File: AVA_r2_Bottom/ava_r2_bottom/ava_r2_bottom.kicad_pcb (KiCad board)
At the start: 2 copper layers, 52 x 72 mm, 29 parts, among them J1 RC_Radio, J2 UART_RxTx_5V, J3 I2C_SdaScl_3V, J4 5V_IN, J5 GND_IN, J6 SER1_SER2, J7 SER3_SER4, J8 SER5_SER6, U1 MPU6500, U2 Teensy4.1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

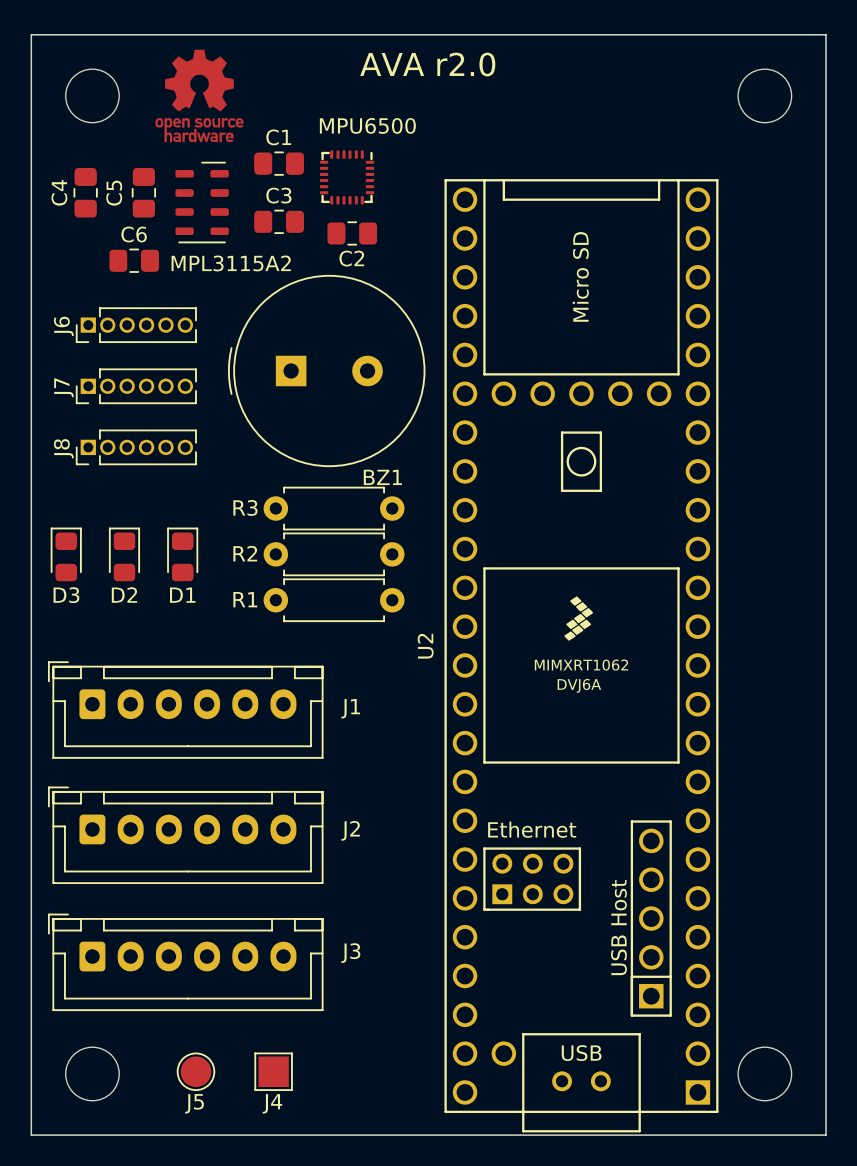
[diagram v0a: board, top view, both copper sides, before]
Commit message: PCB Bottom Complete
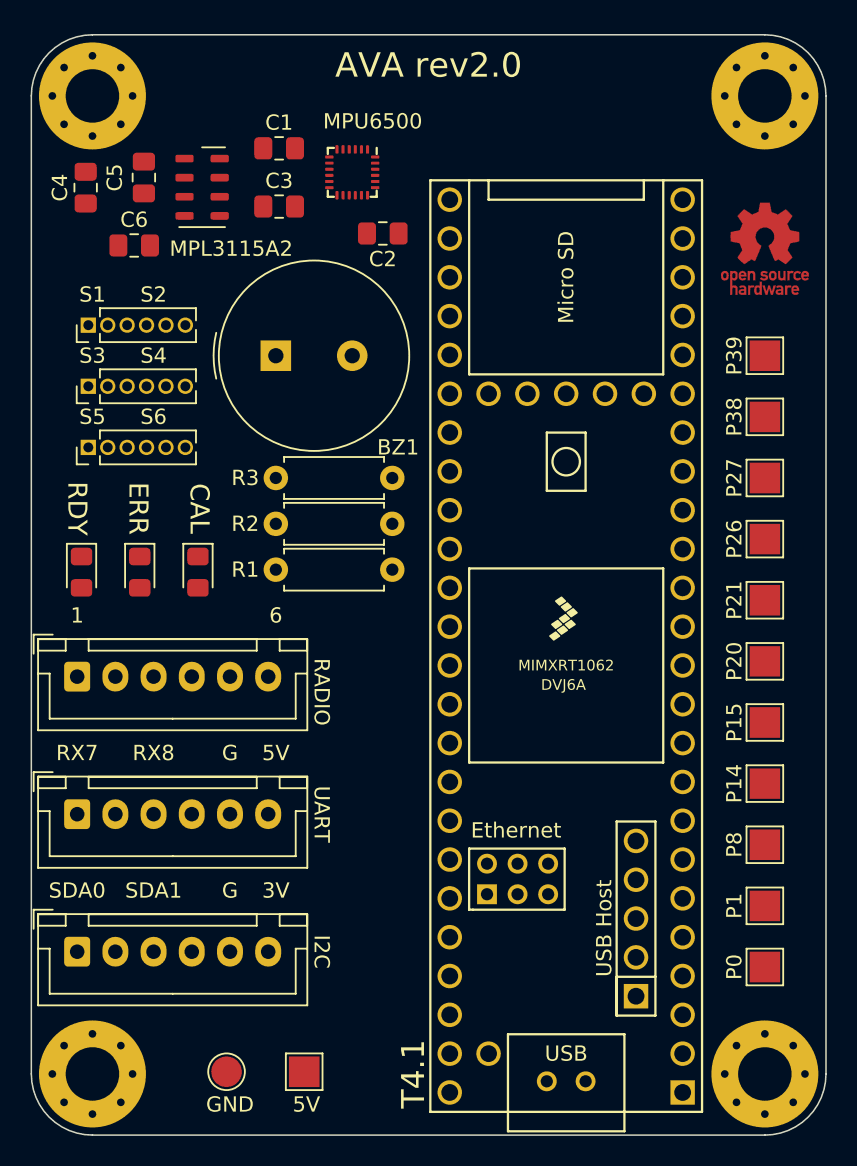
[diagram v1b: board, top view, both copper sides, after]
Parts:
- removed J1: RC_Radio, Connector_JST:JST_XH_B6B-XH-A_1x06_P2.50mm_Vertical
- removed J2: UART_RxTx_5V, Connector_JST:JST_XH_B6B-XH-A_1x06_P2.50mm_Vertical
- removed J3: I2C_SdaScl_3V, Connector_JST:JST_XH_B6B-XH-A_1x06_P2.50mm_Vertical
- removed the REF** at (184.0, 112.0)
- removed the REF** at (228.0, 112.0)
- removed the REF** at (228.0, 48.0)
- removed the REF** at (184.0, 48.0)
- added I2C1: I2C_SdaScl_3V, Connector_JST:JST_XH_B6B-XH-A_1x06_P2.50mm_Vertical, F.Cu at (183.0, 104.0)
- added P0: TestPoint, TestPoint:TestPoint_Pad_2.0x2.0mm, F.Cu at (228.0, 105.0)
- added P1: TestPoint, TestPoint:TestPoint_Pad_2.0x2.0mm, F.Cu at (228.0, 101.0)
- added P14: TestPoint, TestPoint:TestPoint_Pad_2.0x2.0mm, F.Cu at (228.0, 93.0)
- added P15: TestPoint, TestPoint:TestPoint_Pad_2.0x2.0mm, F.Cu at (228.0, 89.0)
- added P20: TestPoint, TestPoint:TestPoint_Pad_2.0x2.0mm, F.Cu at (228.0, 85.0)
- added P21: TestPoint, TestPoint:TestPoint_Pad_2.0x2.0mm, F.Cu at (228.0, 81.0)
- added P26: TestPoint, TestPoint:TestPoint_Pad_2.0x2.0mm, F.Cu at (228.0, 77.0)
- added P27: TestPoint, TestPoint:TestPoint_Pad_2.0x2.0mm, F.Cu at (228.0, 73.0)
- added P38: TestPoint, TestPoint:TestPoint_Pad_2.0x2.0mm, F.Cu at (228.0, 69.0)
- added P39: TestPoint, TestPoint:TestPoint_Pad_2.0x2.0mm, F.Cu at (228.0, 65.0)
- added P8: TestPoint, TestPoint:TestPoint_Pad_2.0x2.0mm, F.Cu at (228.0, 97.0)
- added RADIO1: RC_Radio, Connector_JST:JST_XH_B6B-XH-A_1x06_P2.50mm_Vertical, F.Cu at (183.0, 86.0)
- added REF**: MountingHole_3.5mm_Pad_Via, MountingHole:MountingHole_3.5mm_Pad_Via, F.Cu at (228.0, 112.0)
- added REF**: MountingHole_3.5mm_Pad_Via, MountingHole:MountingHole_3.5mm_Pad_Via, F.Cu at (184.0, 112.0)
- added REF**: MountingHole_3.5mm_Pad_Via, MountingHole:MountingHole_3.5mm_Pad_Via, F.Cu at (184.0, 48.0)
- added REF**: MountingHole_3.5mm_Pad_Via, MountingHole:MountingHole_3.5mm_Pad_Via, F.Cu at (228.0, 48.0)
- added UART1: UART_RxTx_5V, Connector_JST:JST_XH_B6B-XH-A_1x06_P2.50mm_Vertical, F.Cu at (183.0, 95.0)
- moved REF** 38.3 mm to (228.0, 58.0)
- moved C2 2.00 mm to (203.0, 57.0)
- moved J4 2.00 mm to (197.9, 111.9)
- moved J5 2.00 mm to (192.8, 111.9)
- moved R1 2.00 mm to (196.0, 79.0)
- moved R2 2.00 mm to (196.0, 76.0)
- moved R3 2.00 mm to (196.0, 73.0)
- moved BZ1 1.41 mm to (196.0, 65.0)
- moved D1 1.41 mm to (190.9, 79.2)
- moved D2 1.41 mm to (187.1, 79.2)
- moved D3 1.41 mm to (183.3, 79.2)
- moved C1 1.00 mm to (196.2, 51.4)
- moved C3 1.00 mm to (196.2, 55.2)
- moved C5 1.00 mm to (187.4, 53.3)
- moved C6 1.00 mm to (186.7, 57.8)
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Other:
- outline, holes or cut-outs redrawn
- board text added: "1"
- board text added: "3V"
- board text added: "5V"
- board text added: "6"
- board text added: "AVA rev2.0"
- board text added: "CAL"
- board text added: "ERR"
- board text added: "G"
- board text added: "GND"
- board text added: "I2C"
- board text added: "RADIO"
- board text added: "RDY"
- board text added: "RX7"
- board text added: "RX8"
- board text added: "S1"
- board text added: "S2"
- board text added: "S3"
- board text added: "S4"
- board text added: "S5"
- board text added: "S6"
- board text added: "SDA0"
- board text added: "SDA1"
- board text added: "T4.1"
- board text added: "UART"
- board text removed: "AVA r2.0"

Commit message: added mpu6050
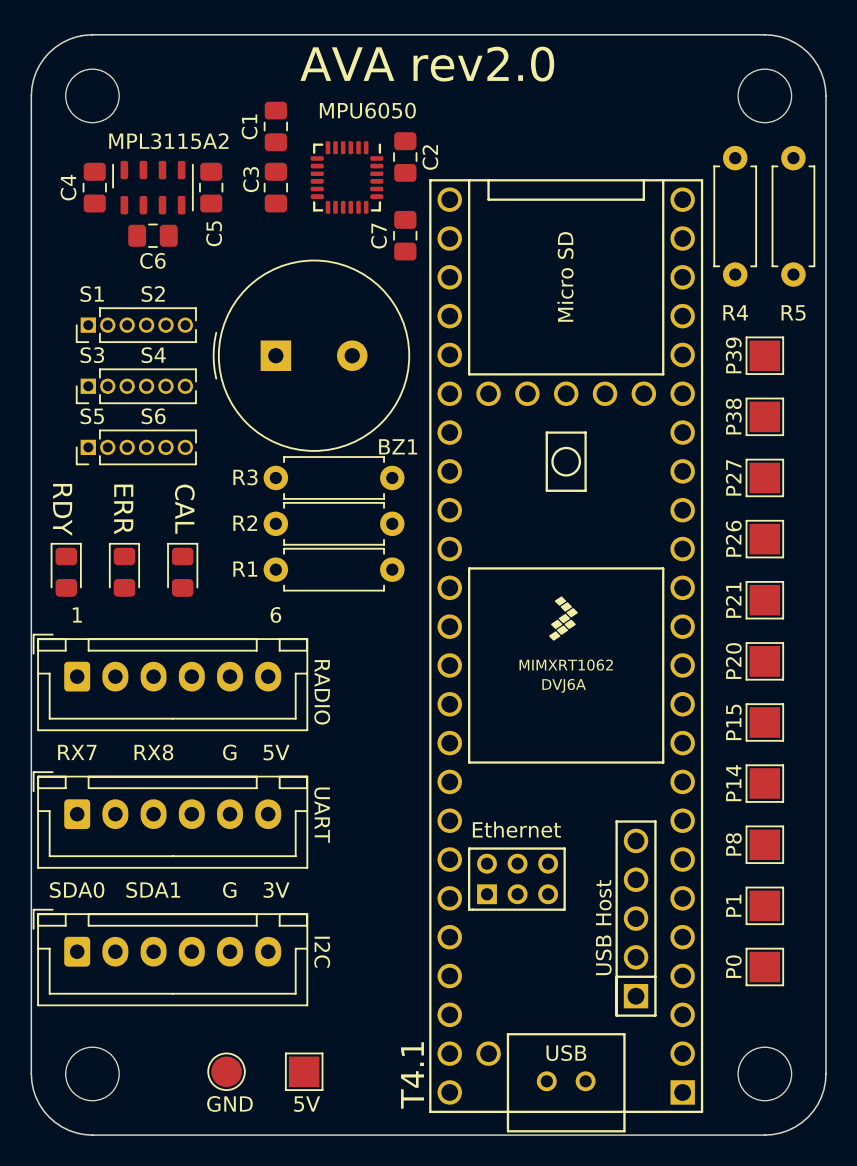
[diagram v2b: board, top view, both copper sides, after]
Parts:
- removed the REF** at (228.0, 112.0)
- removed the REF** at (184.0, 112.0)
- removed the REF** at (184.0, 48.0)
- removed the REF** at (228.0, 48.0)
- removed the REF** at (228.0, 58.0)
- removed U1: MPU6500, Sensor_Motion:InvenSense_QFN-24_3x3mm_P0.4mm
- added C7: 2200pF, Capacitor_SMD:C_0805_2012Metric_Pad1.18x1.45mm_HandSolder, F.Cu at (204.5, 57.1)
- added MPU6050: MPU-6050, Sensor_Motion:InvenSense_QFN-24_4x4mm_P0.5mm, F.Cu at (200.7, 53.3)
- added R4: 4.7K, Resistor_THT:R_Axial_DIN0207_L6.3mm_D2.5mm_P7.62mm_Horizontal, F.Cu at (226.1, 59.7)
- added R5: 4.7K, Resistor_THT:R_Axial_DIN0207_L6.3mm_D2.5mm_P7.62mm_Horizontal, F.Cu at (229.9, 59.7)
- added REF**: MountingHole_3.5mm, MountingHole:MountingHole_3.5mm, F.Cu at (228.0, 112.0)
- added REF**: MountingHole_3.5mm, MountingHole:MountingHole_3.5mm, F.Cu at (184.0, 112.0)
- added REF**: MountingHole_3.5mm, MountingHole:MountingHole_3.5mm, F.Cu at (228.0, 48.0)
- added REF**: MountingHole_3.5mm, MountingHole:MountingHole_3.5mm, F.Cu at (184.0, 48.0)
- C1: value 10nF -> 0.1uF
- moved C2 5.21 mm to (204.5, 52.0), turned to 270 degrees
- moved C5 4.45 mm to (191.8, 54.0)
- moved U3 3.22 mm to (188.0, 54.0), turned to 90 degrees
- moved C1 1.45 mm to (196.0, 50.0), turned to 90 degrees
- moved C6 1.38 mm to (188.0, 57.1), turned to 180 degrees
- moved C3 1.26 mm to (196.0, 54.0), turned to 270 degrees
- moved D1 1.00 mm to (189.9, 79.2)
- moved D2 1.00 mm to (186.1, 79.2)
- moved D3 1.00 mm to (182.3, 79.2)
- moved C4 0.59 mm to (184.2, 54.0)
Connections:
- C1 pad 1: GND -> +3V3
- C1 pad 2: +3V3 -> GND
- C3 pad 1: GND -> Net-(C3-Pad1)
- C3 pad 2: Net-(C3-Pad2) -> GND

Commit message: Submitted PCB Design
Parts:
- renumbered REF** to hole1, REF** to hole2, REF** to hole3, REF** to hole4
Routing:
- net GND: track 0.00 -> 201.9 mm
- net +3V3: track 0.00 -> 170.1 mm, vias 0 -> 2
- net I2C0_SCL: track 0.00 -> 136.5 mm
- net I2C0_SDA: track 0.00 -> 127.3 mm, vias 0 -> 2
- net +5V: track 0.00 -> 85.8 mm
- net SERVO1_PWM: track 0.00 -> 84.3 mm
- net UART7_TX: track 0.00 -> 82.1 mm
- net SERVO2_PWM: track 0.00 -> 74.6 mm
- net SERVO3_PWM: track 0.00 -> 72.7 mm
- net UART7_RX: track 0.00 -> 68.8 mm
- net UART8_RX: track 0.00 -> 64.1 mm
- net SERVO4_PWM: track 0.00 -> 63.8 mm
- net UART8_TX: track 0.00 -> 63.7 mm
- net SERVO5_PWM: track 0.00 -> 61.6 mm
- net SERVO6_PWM: track 0.00 -> 54.8 mm
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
